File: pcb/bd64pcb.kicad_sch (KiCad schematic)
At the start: 237 parts, among them J1 USB_C_Receptacle_USB2.0, SW1 SW_Push, U1 ATmega32U4-MU, U2 MCP23017_ML, U3 IS31FL3733-QF, Y1 16MHz

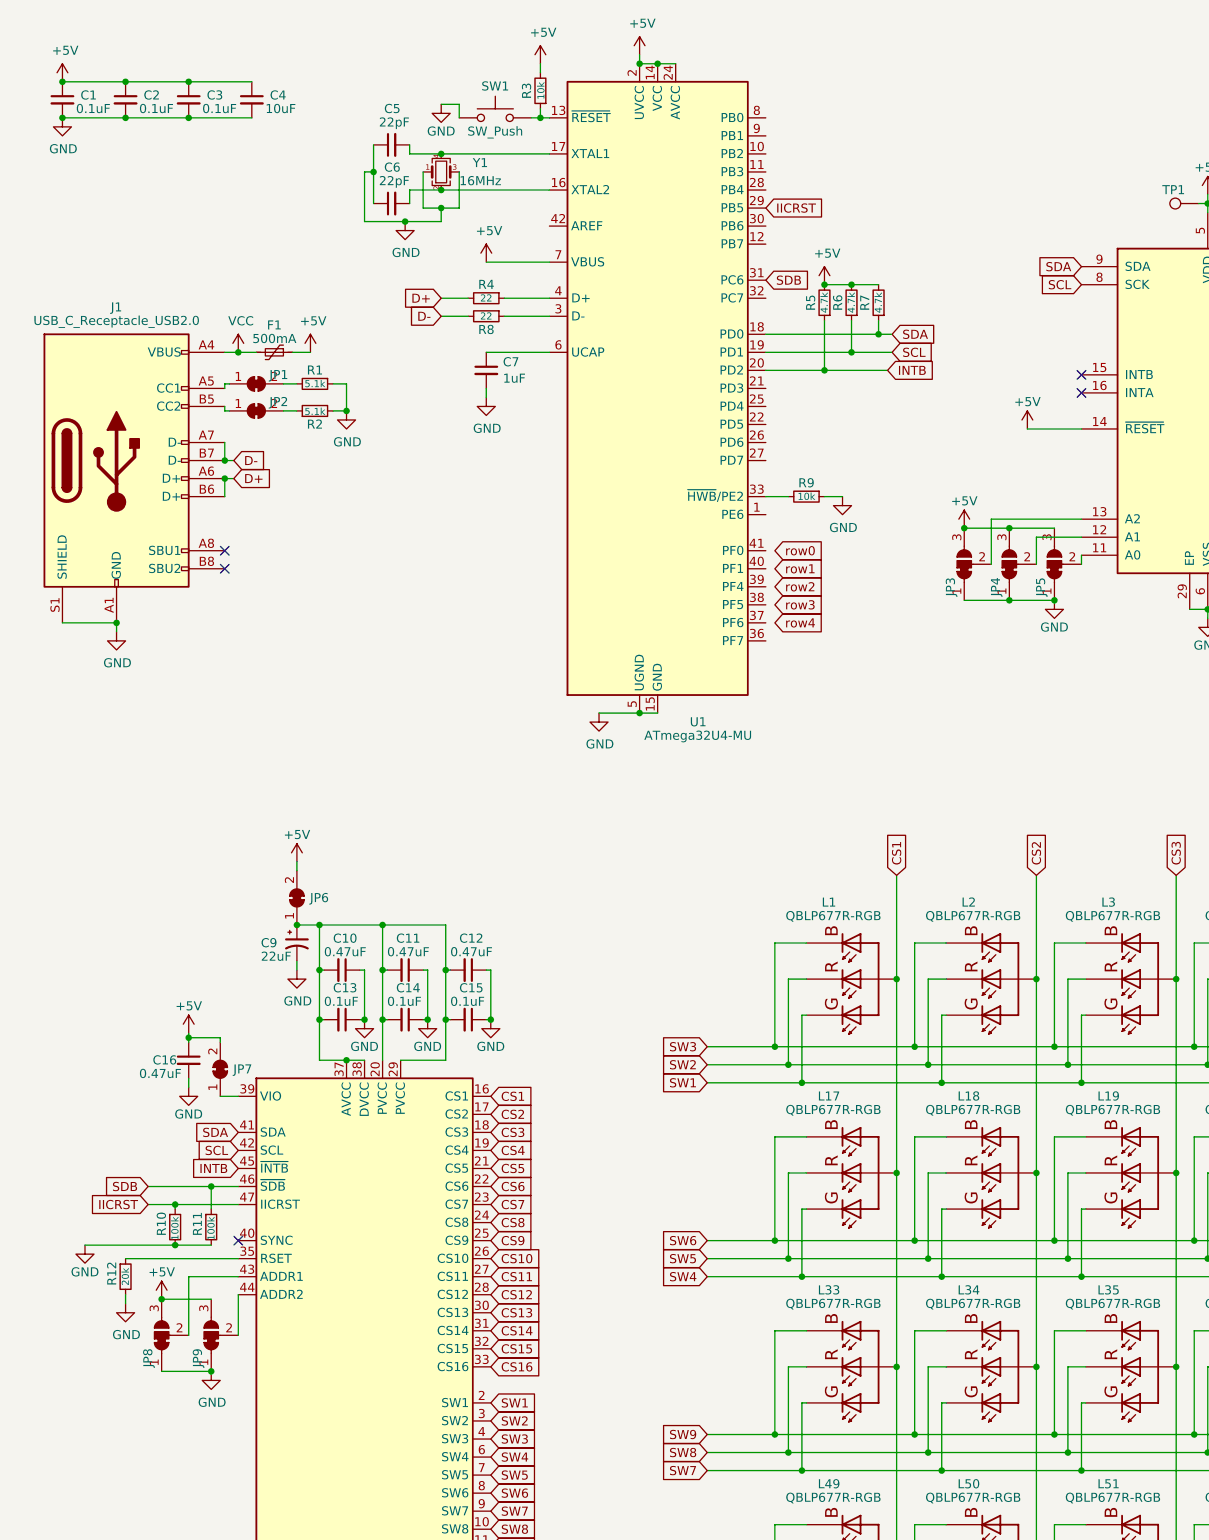
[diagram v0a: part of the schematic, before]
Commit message: removed solder jumpers. addresses are now fixed.
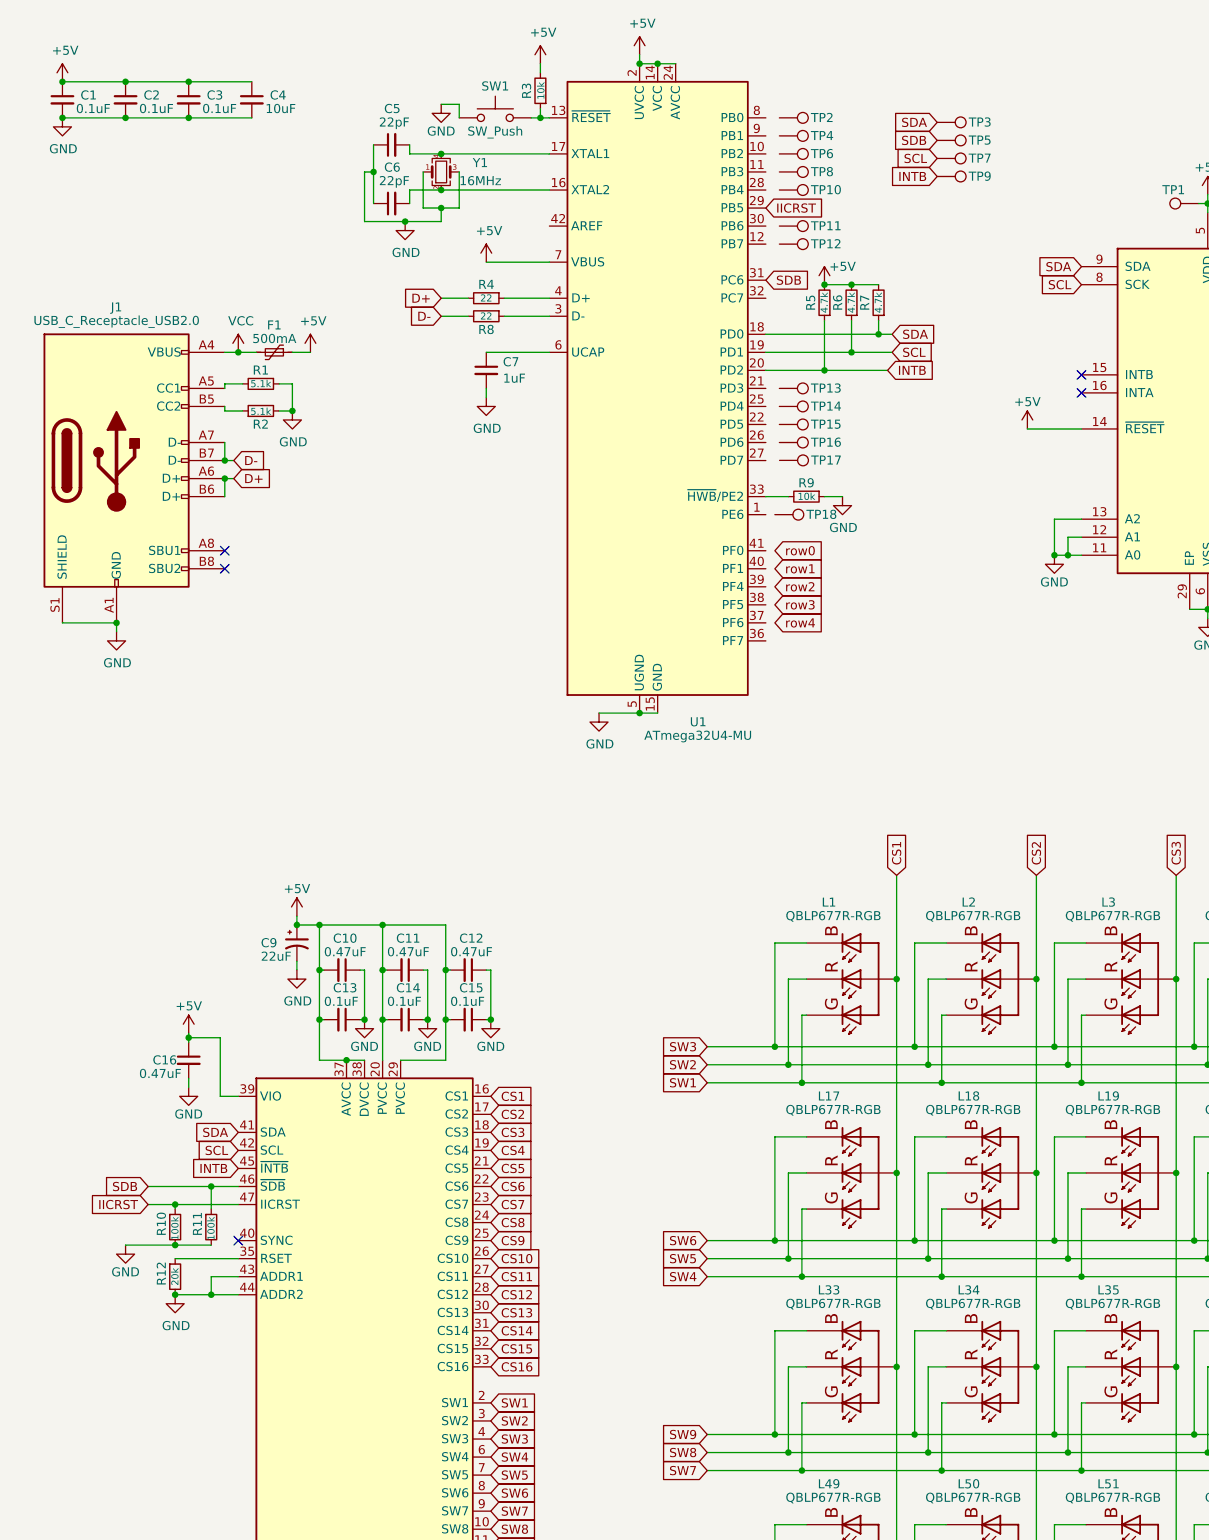
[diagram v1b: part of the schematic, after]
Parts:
- removed JP1, JP2, JP6, JP7: SolderJumper_2_Bridged, Jumper:SolderJumper-2_P1.3mm_Bridged_RoundedPad1.0x1.5mm, symbol Jumper:SolderJumper_2_Bridged
- removed JP3, JP4, JP5, JP8, JP9: SolderJumper_3_Bridged12, Jumper:SolderJumper-3_P1.3mm_Bridged12_RoundedPad1.0x1.5mm, symbol bd64pcb-rescue:SolderJumper_3_Bridged12-Jumper
- added TP10, TP11, TP12, TP13, TP14, TP15, TP16, TP17, TP18, TP2, TP3, TP4, TP5, TP6, TP7, TP8, TP9: TestPoint, TestPoint:TestPoint_Plated_Hole_D2.0mm, symbol Connector:TestPoint
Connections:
- net +5V: now also C10.2, C11.2, C12.2, C13.2, C14.2, C15.2, C9.1, U3.20 (PVCC), U3.29 (PVCC), U3.37 (AVCC), U3.38 (DVCC), U3.39 (VIO)
- net GND: now also U2.11 (A0), U2.12 (A1), U2.13 (A2), U3.43 (ADDR1), U3.44 (ADDR2)
- net INTB: now also TP9.1
- net SCL: now also TP7.1
- net SDA: now also TP3.1
- net SDB: now also TP5.1
- net at J1.A5 (CC1): now also R1.2
- net at J1.B5 (CC2): now also R2.1
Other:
- moved on the sheet: R1, R12, R2

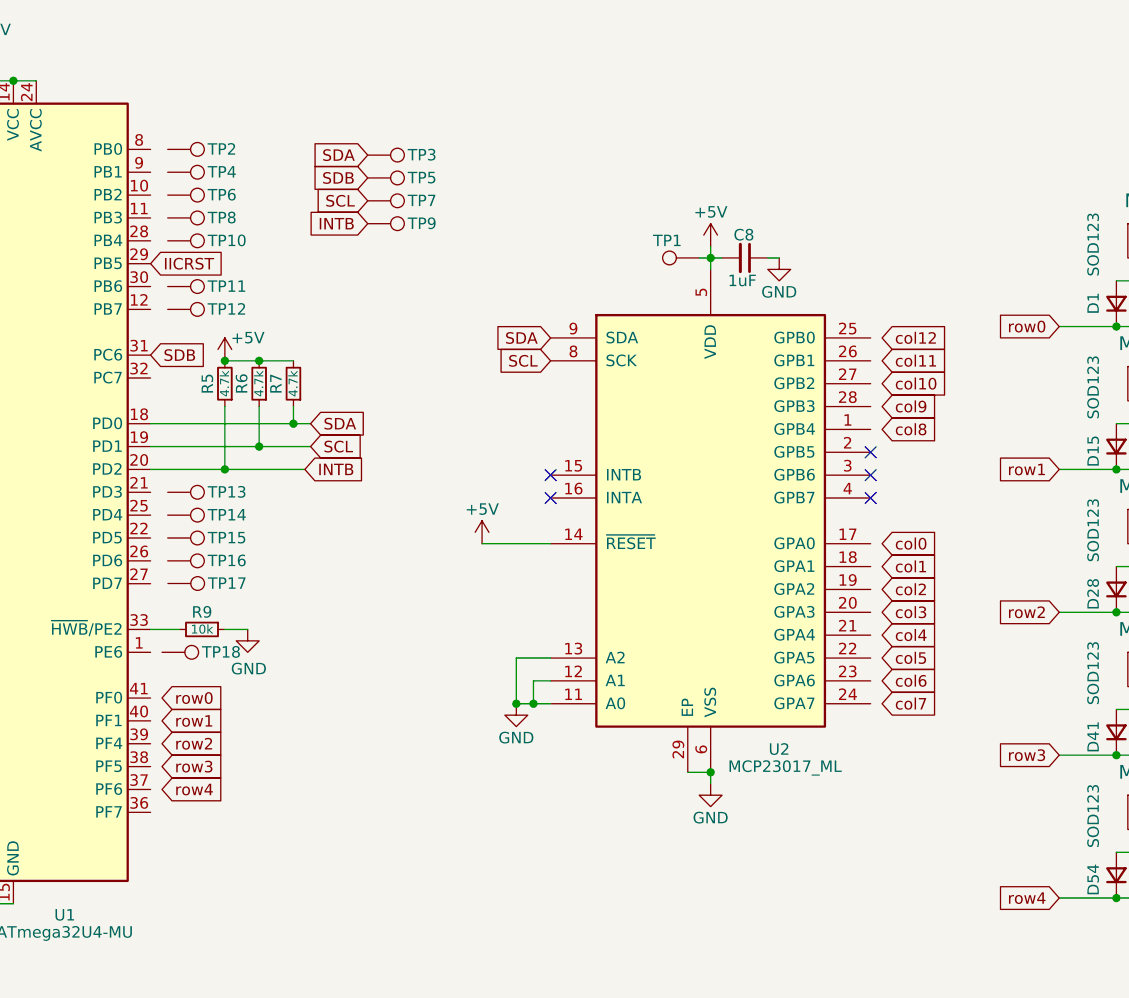
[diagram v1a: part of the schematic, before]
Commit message: mcp delet
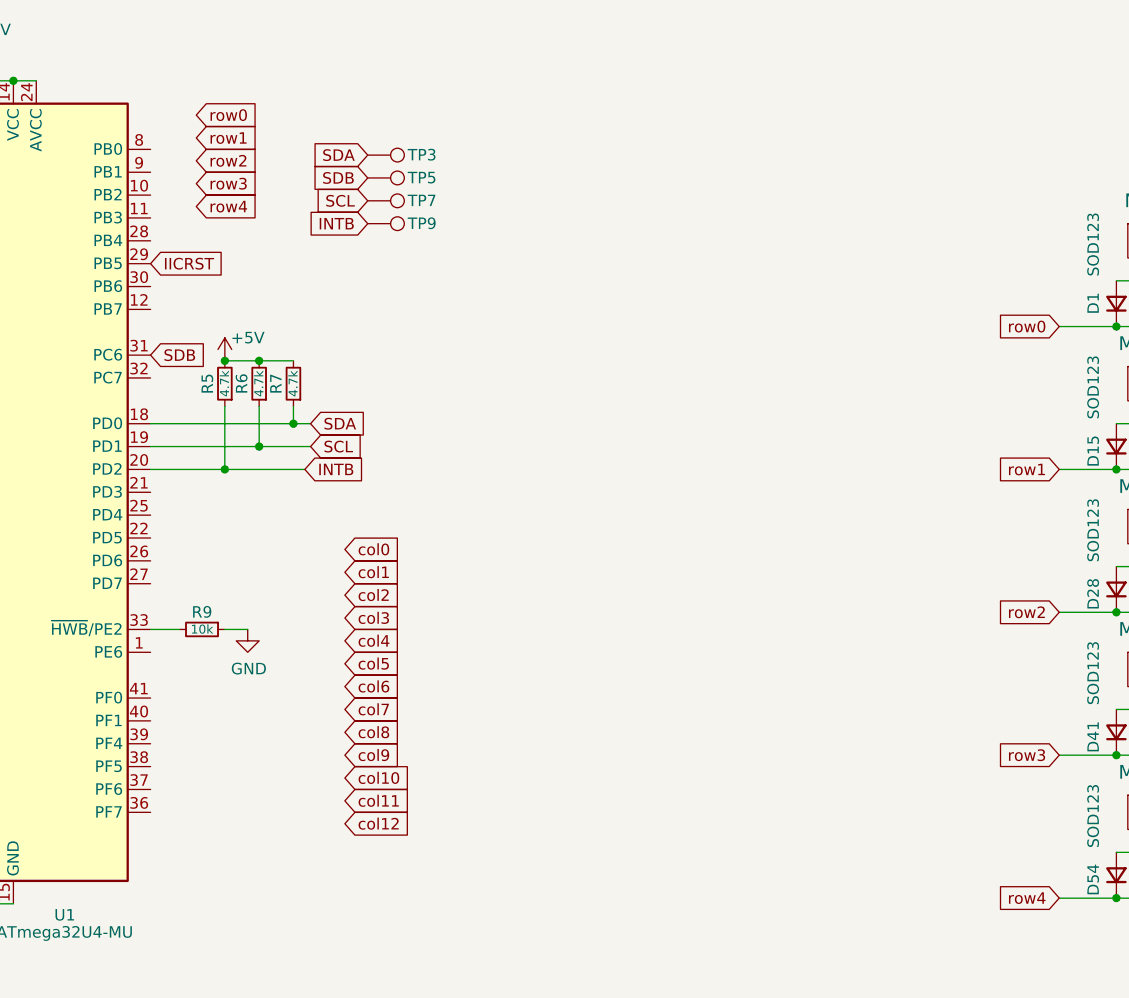
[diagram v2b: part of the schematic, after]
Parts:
- removed C8: 1uF, Capacitor_SMD:C_0805_2012Metric, symbol Device:C_Small
- removed TP1, TP10, TP11, TP12, TP13, TP14, TP15, TP16, TP17, TP18, TP2, TP4, TP6, TP8: TestPoint, TestPoint:TestPoint_Plated_Hole_D2.0mm, symbol Connector:TestPoint
- removed U2: MCP23017_ML, Package_DFN_QFN:QFN-28-1EP_6x6mm_P0.65mm_EP4.25x4.25mm, symbol Interface_Expansion:MCP23017_ML
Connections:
- no-connect marks 8 -> 3

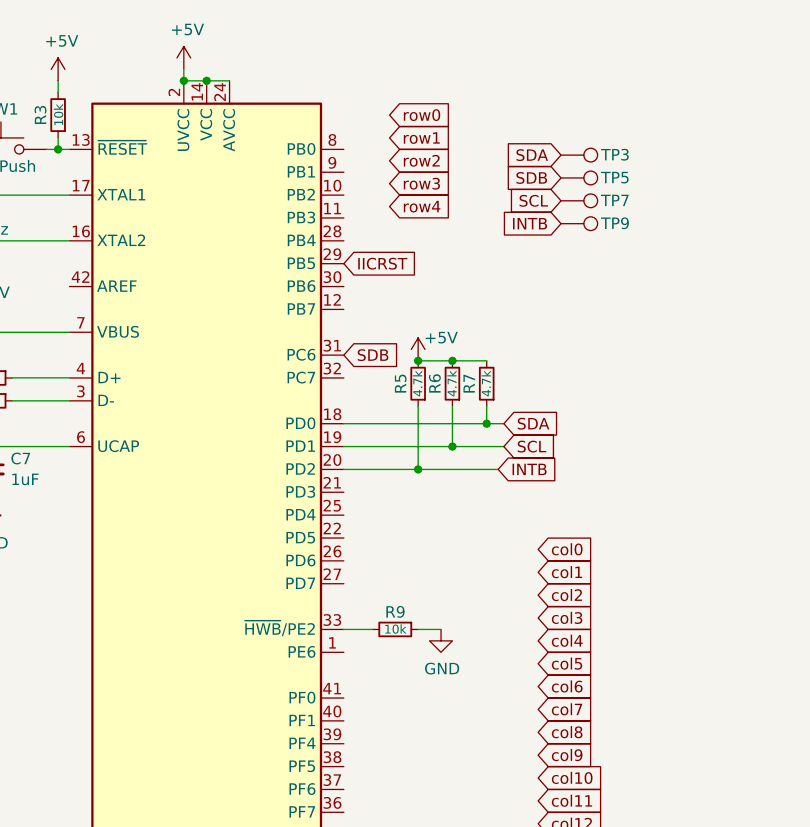
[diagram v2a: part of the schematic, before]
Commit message: switch rows routed
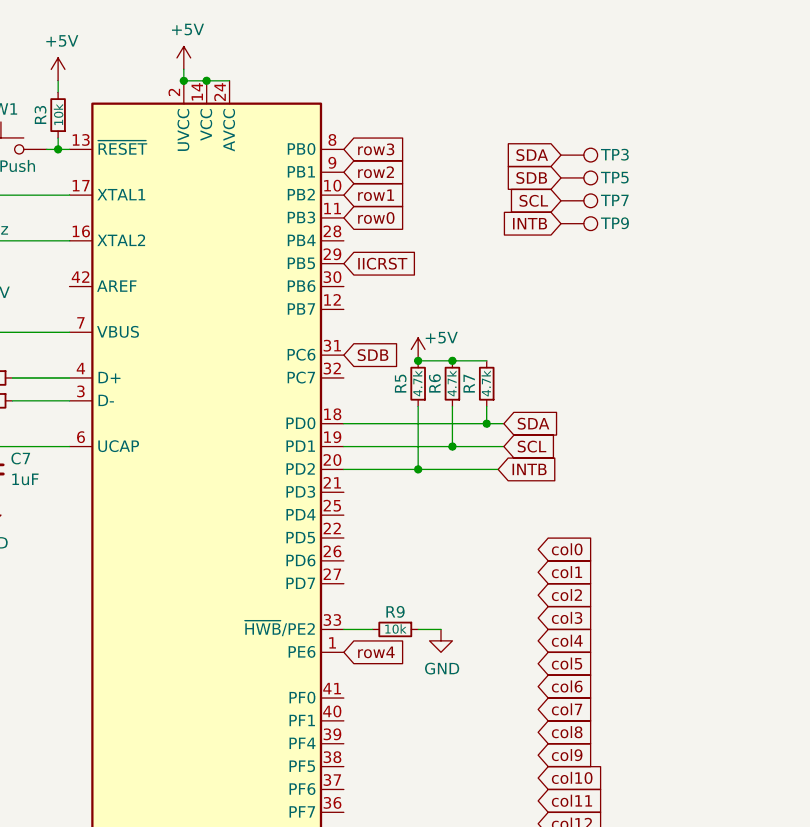
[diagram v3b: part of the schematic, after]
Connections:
- net row0: now also U1.11 (PB3)
- net row1: now also U1.10 (PB2)
- net row2: now also U1.9 (PB1)
- net row3: now also U1.8 (PB0)
- net row4: now also U1.1 (PE6)
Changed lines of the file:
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@@
     )
   )
-  (global_label "row2" (shape input) (at 128.27 41.91 0) (fields_autoplaced)
-    (effects (font (size 1.27 1.27)) (justify left))
-    (property "Intersheet References" "${INTERSHEET_REFS}" (id 0) (at 3.81 -64.77 0)
+  (global_label "row2" (shape input) (at 123.19 43.18 0) (fields_autoplaced)
+    (effects (font (size 1.27 1.27)) (justify left))
+    (property "Intersheet References" "${INTERSHEET_REFS}" (id 0) (at -1.27 -63.5 0)
       (effects (font (size 1.27 1.27)) hide)
     )
@@
     )
   )
-  (global_label "row4" (shape input) (at 128.27 46.99 0) (fields_autoplaced)
-    (effects (font (size 1.27 1.27)) (justify left))
-    (property "Intersheet References" "${INTERSHEET_REFS}" (id 0) (at 3.81 -64.77 0)
+  (global_label "row4" (shape input) (at 123.19 96.52 0) (fields_autoplaced)
+    (effects (font (size 1.27 1.27)) (justify left))
+    (property "Intersheet References" "${INTERSHEET_REFS}" (id 0) (at -1.27 -15.24 0)
       (effects (font (size 1.27 1.27)) hide)
     )
@@
     )
   )
-  (global_label "row3" (shape input) (at 128.27 44.45 0) (fields_autoplaced)
-    (effects (font (size 1.27 1.27)) (justify left))
-    (property "Intersheet References" "${INTERSHEET_REFS}" (id 0) (at 3.81 -64.77 0)
+  (global_label "row3" (shape input) (at 123.19 40.64 0) (fields_autoplaced)
+    (effects (font (size 1.27 1.27)) (justify left))
+    (property "Intersheet References" "${INTERSHEET_REFS}" (id 0) (at -1.27 -68.58 0)
       (effects (font (size 1.27 1.27)) hide)
     )
@@
     )
   )
-  (global_label "row0" (shape input) (at 128.27 36.83 0) (fields_autoplaced)
-    (effects (font (size 1.27 1.27)) (justify left))
-    (property "Intersheet References" "${INTERSHEET_REFS}" (id 0) (at 3.81 -64.77 0)
+  (global_label "row0" (shape input) (at 123.19 48.26 0) (fields_autoplaced)
+    (effects (font (size 1.27 1.27)) (justify left))
+    (property "Intersheet References" "${INTERSHEET_REFS}" (id 0) (at -1.27 -53.34 0)
       (effects (font (size 1.27 1.27)) hide)
     )
@@
     )
   )
-  (global_label "row1" (shape input) (at 128.27 39.37 0) (fields_autoplaced)
-    (effects (font (size 1.27 1.27)) (justify left))
-    (property "Intersheet References" "${INTERSHEET_REFS}" (id 0) (at 3.81 -64.77 0)
-      (effects (font (size 1.27 1.27)) hide)
-    )
+  (global_label "row1" (shape input) (at 123.19 45.72 0) (fields_autoplaced)
+    (effects (font (size 1.27 1.27)) (justify left))
+    (property "Intersheet References" "${INTERSHEET_REFS}" (id 0) (at -1.27 -58.42 0)
+      (effects (font (size 1.27 1.27)) hide)
+    )
